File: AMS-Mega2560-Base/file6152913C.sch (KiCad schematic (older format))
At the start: 25 parts, among them IC17 DS3231SN#, IC18 MAX232CPE+, Q10 2N7000, Q11 2N7000, Q12 2N7000, Q7 IRF510, Q8 IRF510, Q9 IRF510, U3 S8411-45R

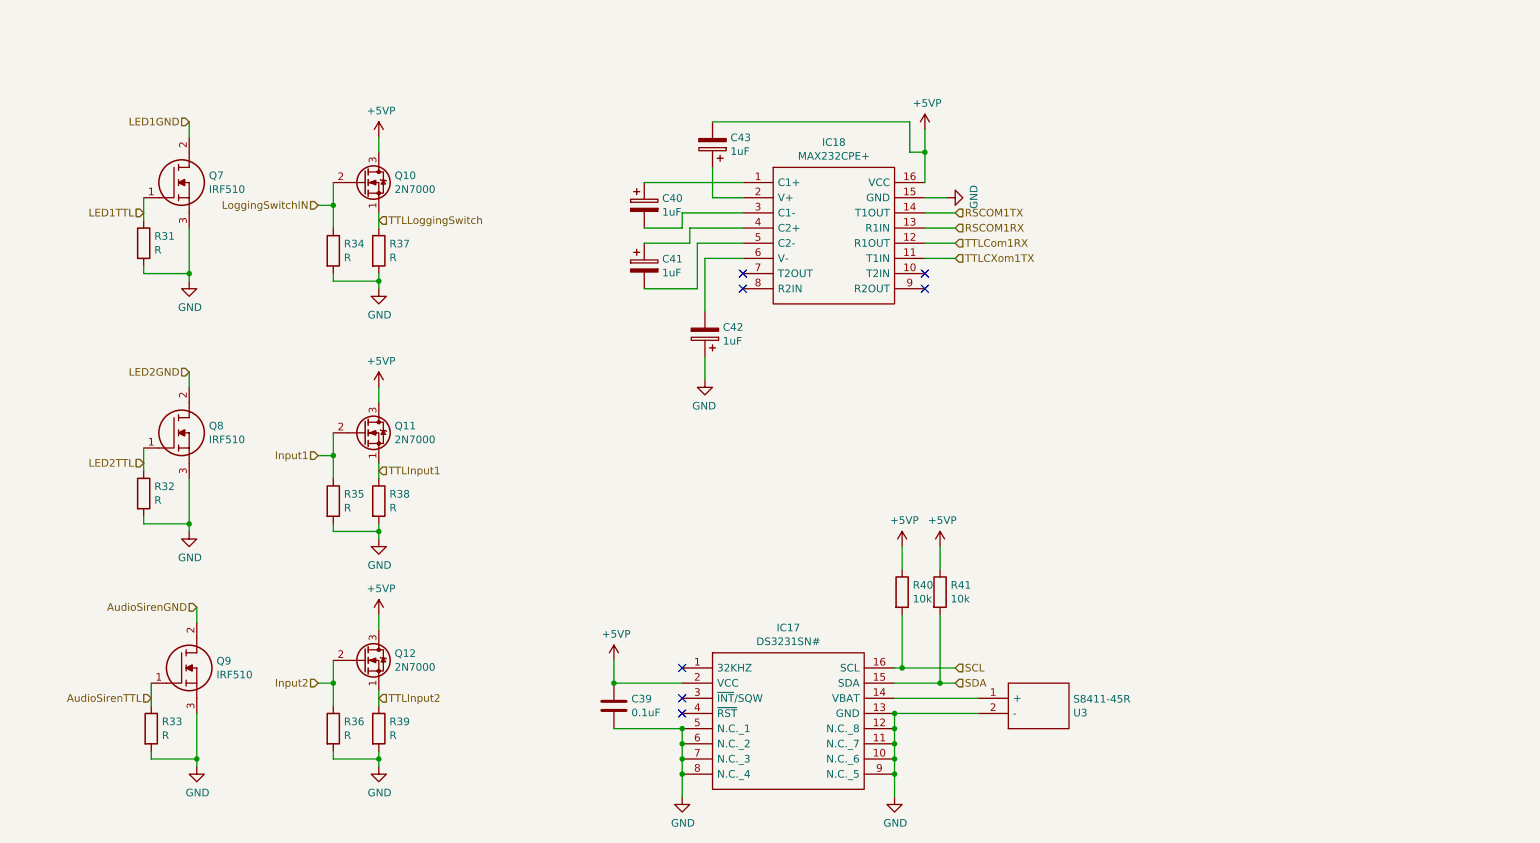
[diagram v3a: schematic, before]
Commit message: upgrading this to 6.0 and moving the vacuum sensors to a daughter board project.
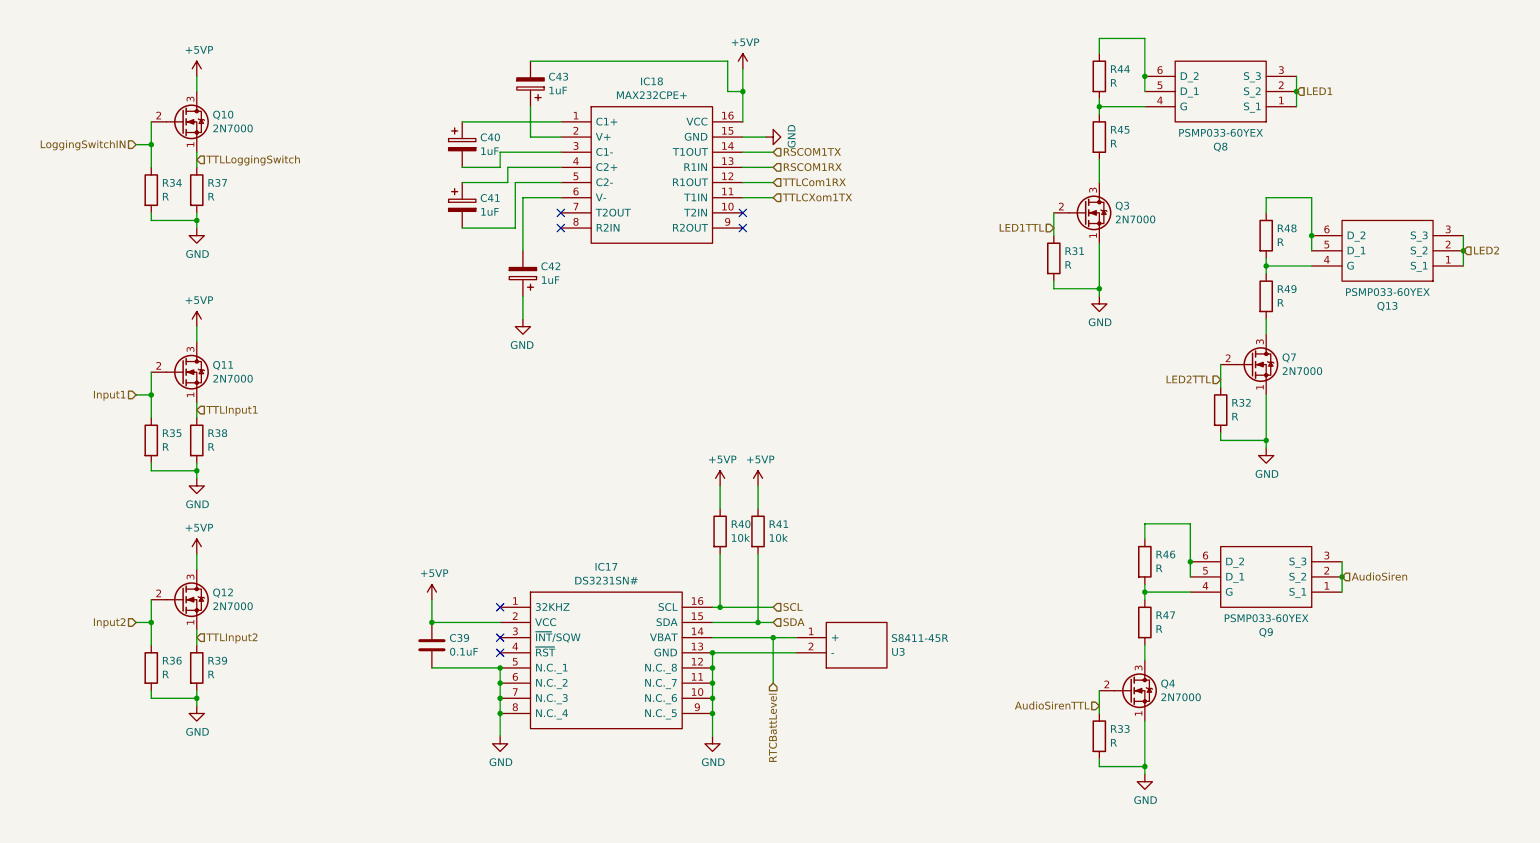
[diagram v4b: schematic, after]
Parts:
- removed Q7, Q8, Q9: IRF510, SamacSys_Parts:TO254P465X1024X2050-3P, symbol SamacSys_Parts:IRF510
- added Q13, Q8, Q9: PSMP033-60YEX, PSMP03360YEX, symbol SamacSys_Parts:PSMP033-60YEX
- added Q3, Q4, Q7: 2N7000, Package_TO_SOT_THT:TO-92_Inline, symbol Transistor_FET:2N7000
- added R44, R45, R46, R47, R48, R49: R, Resistor_THT:R_Axial_DIN0207_L6.3mm_D2.5mm_P5.08mm_Vertical, symbol Device:R
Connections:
- net AudioSirenTTL: now also Q4.2 (G)
- net GND: now also Q3.1 (S), Q4.1 (S), Q7.1 (S)
- net LED1TTL: now also Q3.2 (G)
- net LED2TTL: now also Q7.2 (G)
- net RTCBattLevel: now reaches IC17.14 (VBAT), U3.1 (+)
- new net: Q8.4 (G), R44.2, R45.1
- new net: Q8.5 (D_1), Q8.6 (D_2), R44.1
- new net: Q3.3 (D), R45.2
- new net: Q7.3 (D), R49.2
- new net: Q4.3 (D), R47.2
- new net: Q13.4 (G), R48.2, R49.1
- new net: Q13.5 (D_1), Q13.6 (D_2), R48.1
- new net: Q9.4 (G), R46.2, R47.1
- new net: Q9.5 (D_1), Q9.6 (D_2), R46.1
- new net AudioSiren: Q9.1 (S_1), Q9.2 (S_2), Q9.3 (S_3)
- new net LED1: Q8.1 (S_1), Q8.2 (S_2), Q8.3 (S_3)
- new net LED2: Q13.1 (S_1), Q13.2 (S_2), Q13.3 (S_3)
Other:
- moved on the sheet: C39, C40, C41, C42, C43, IC17, IC18, Q10, Q11, Q12, R31, R32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
